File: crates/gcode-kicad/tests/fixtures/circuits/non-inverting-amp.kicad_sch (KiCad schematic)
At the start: 3 parts, among them U1 LM321

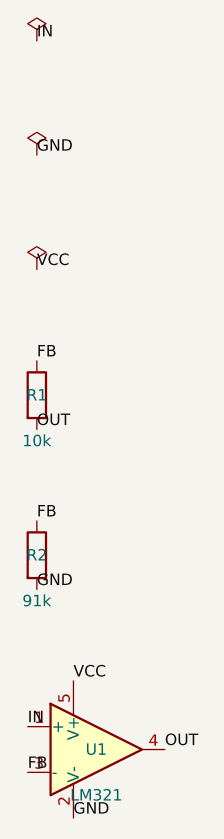
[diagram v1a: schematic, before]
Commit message: R1: gcode-sim crate — SPICE netlist generation, ngspice driver, metric analysis
New crate crates/gcode-sim:
- models: lib_id -> SPICE card + behavioural macromodels (LM321 single-pole
  opamp, Q_NMOS level-1, LED, L7805, thermistor); unknown devices are rejected
- netlist: deterministic deck from NetlistIr; GND -> node 0, sanitised node names
  with collision detection, stimuli from the analysis config, wrdata control block
- runner: ngspice probe/version gate, batch execution, waveform retrieval parsed
  BY COLUMN NAME (which is what makes .op's placeholder scale column harmless)
- analysis: pure metric extraction (dc, gain, shape-aware -3dB, rise time,
  ripple, min/max) plus expectation checking with Chinese explanations
- artifacts: deterministic CSV and dependency-free SVG (Bode + time domain)
- recipes: 11 recipes over all 10 catalog circuits with analytically derived
  expectations and documented tolerances

Real findings from actually simulating (all fixed):
- non-inverting-amp was wired for gain 1.11, not 10.1 (feedback resistors swapped)
- MOSFETs need the M card, not Q (Q is a BJT); bulk ties to source
- ngspice level-1 MOS rejects Cgs/Cgd (wants CGSO/CGDO)
- ngspice vp() returns radians, not degrees
- with the switch off, the drain is a floating node; measure the supply side
- Sallen-Key Q was 0.34 (overdamped) -> values swapped for Q~0.74
- thermistor value must be numeric to be simulatable

Acceptance: 11/11 recipes, 12/12 metrics PASS against ngspice-42; R0 still
10/10 KR1 and 146 workspace tests green.
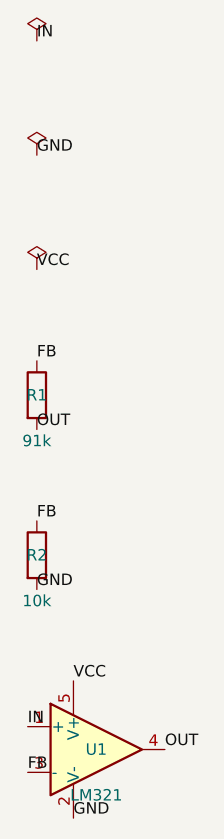
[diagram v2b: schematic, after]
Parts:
- R1: value 10k -> 91k
- R2: value 91k -> 10k
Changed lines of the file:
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@@
     (instances (project
   "gcode"
-  (path "/e237412c-b614-523e-acce-1b91ac626522" (reference "#FLG1") (unit 1))
+  (path "/dfd43e20-bc50-5246-9481-410ebfd3ef6c" (reference "#FLG1") (unit 1))
 ))
   )
@@
     (instances (project
   "gcode"
-  (path "/e237412c-b614-523e-acce-1b91ac626522" (reference "#FLG2") (unit 1))
+  (path "/dfd43e20-bc50-5246-9481-410ebfd3ef6c" (reference "#FLG2") (unit 1))
 ))
   )
@@
     (instances (project
   "gcode"
-  (path "/e237412c-b614-523e-acce-1b91ac626522" (reference "#FLG3") (unit 1))
+  (path "/dfd43e20-bc50-5246-9481-410ebfd3ef6c" (reference "#FLG3") (unit 1))
 ))
   )
@@
     (property
       "Value"
-      "10k"
+      "91k"
       (at 77.216 97.79 0)
       (show_name no)
@@
     (instances (project
   "gcode"
-  (path "/e237412c-b614-523e-acce-1b91ac626522" (reference "R1") (unit 1))
+  (path "/dfd43e20-bc50-5246-9481-410ebfd3ef6c" (reference "R1") (unit 1))
 ))
   )
@@
     (property
       "Value"
-      "91k"
+      "10k"
       (at 77.216 115.57 0)
       (show_name no)
@@
     (instances (project
   "gcode"
-  (path "/e237412c-b614-523e-acce-1b91ac626522" (reference "R2") (unit 1))
+  (path "/dfd43e20-bc50-5246-9481-410ebfd3ef6c" (reference "R2") (unit 1))
 ))
   )
@@
     (instances (project
   "gcode"
-  (path "/e237412c-b614-523e-acce-1b91ac626522" (reference "U1") (unit 1))
-))
-  )
+  (path "/dfd43e20-bc50-5246-9481-410ebfd3ef6c" (reference "U1") (unit 1))
+))
+  )
